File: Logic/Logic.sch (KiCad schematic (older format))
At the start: 8 parts, among them J1 MC_CAN, J12 GPIO_I2C, J2 IMU, J3 RTC, J4 GLV_I2C, J8 GLV_24V

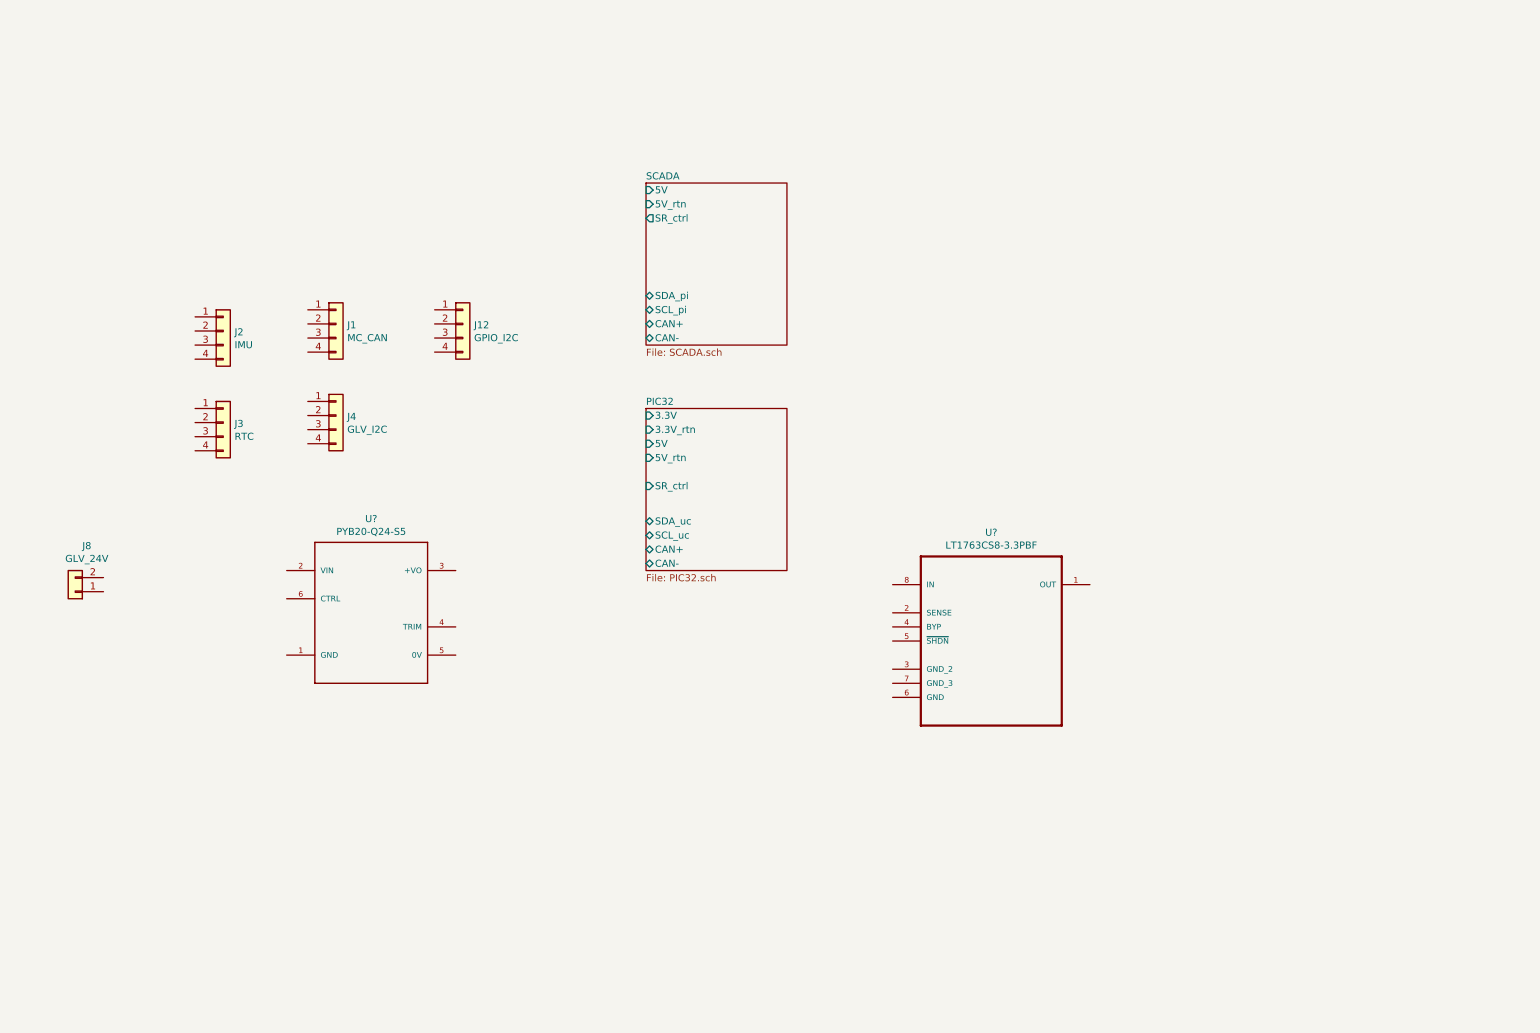
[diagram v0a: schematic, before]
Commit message: Finished Logic Board schematic and removed old schematics
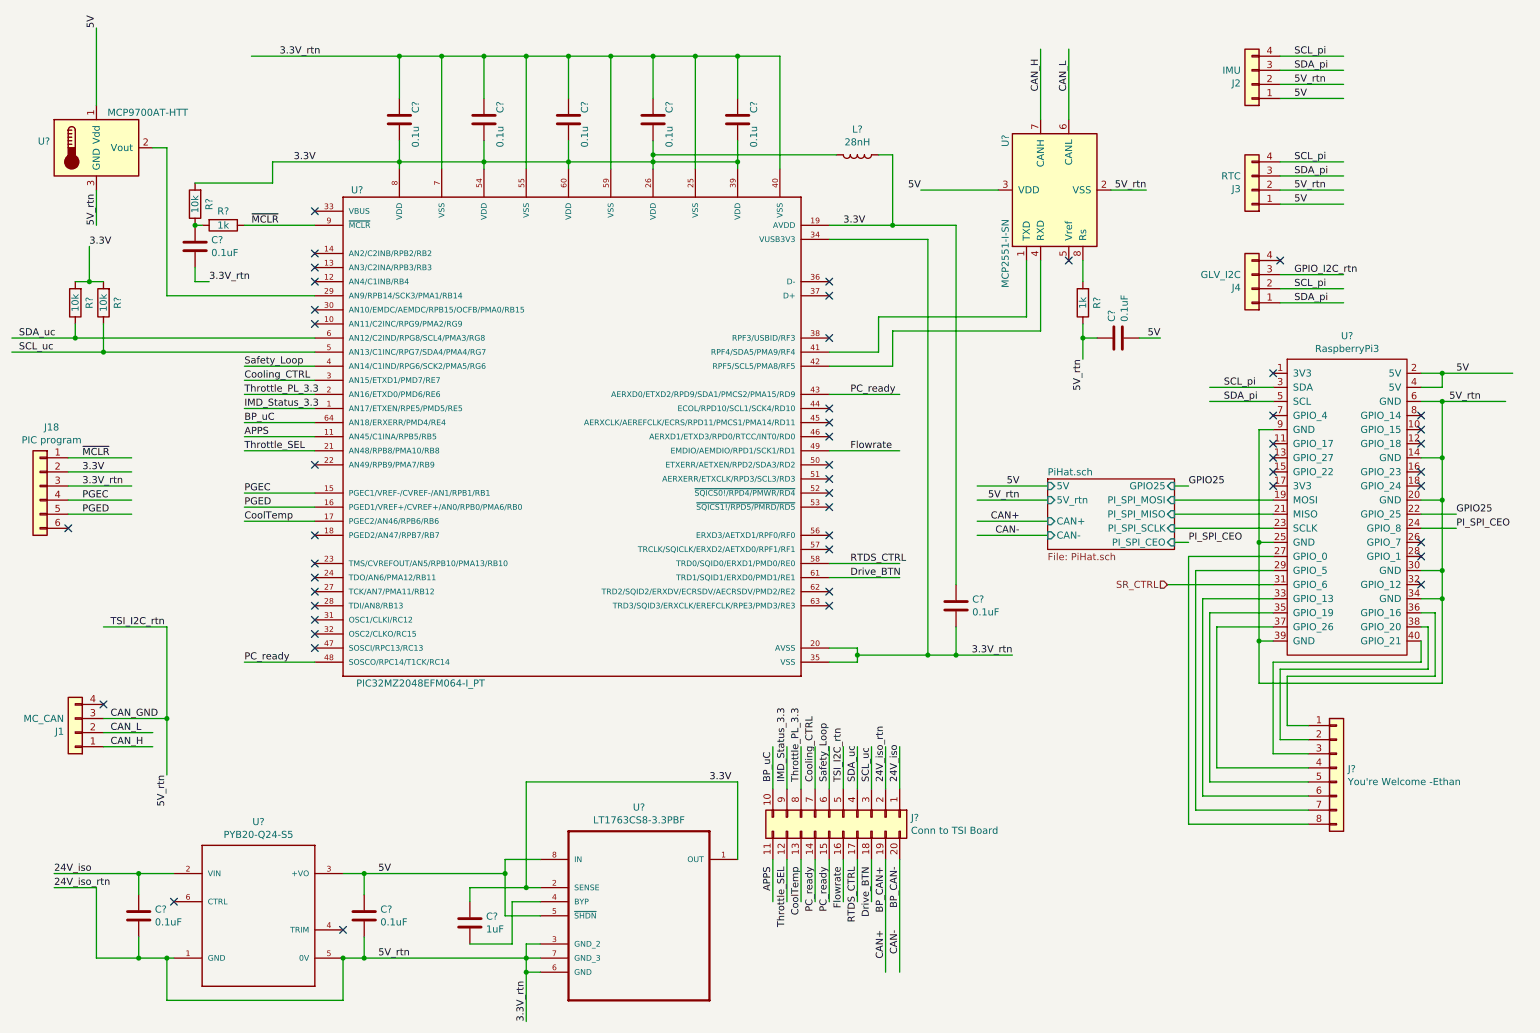
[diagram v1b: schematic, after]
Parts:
- removed J12: GPIO_I2C, symbol Connector_Generic:Conn_01x04
- removed J8: GLV_24V, symbol Connector_Generic:Conn_01x02
- added C? (x5): 0.1uF, symbol Device:C
- added C?: 1uF, symbol Device:C
- added C? (x5): 0.1u, symbol Device:C
- added J18: PIC program, symbol Connector_Generic:Conn_01x06
- added J?: You're Welcome -Ethan, symbol Connector_Generic:Conn_01x08
- added J?: Conn to TSI Board, symbol Connector_Generic:Conn_02x10_Counter_Clockwise
- added L?: 28nH, symbol Device:L
- added R? (x3): 10k, symbol Device:R
- added R? (x2): 1k, symbol Device:R
- added U?: RaspberryPi3, Lafayette_Electric_Car_Footprints:RaspberryPi3, symbol Lafayette_Electric_Car_Internals:RaspberryPi3
- added U?: MCP9700AT-HTT, Package_TO_SOT_SMD:SOT-23, symbol Sensor_Temperature:MCP9700AT-HTT
- added U?: MCP2551-I-SN, Package_SO:SOIC-8_3.9x4.9mm_P1.27mm, symbol Interface_CAN_LIN:MCP2551-I-SN
- added U?: PIC32MZ2048EFM064-I_PT, QFP50P1200X1200X120-64N, symbol PIC32MZ2048EFM064-I_PT:PIC32MZ2048EFM064-I_PT
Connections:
- net labels added: 24V_iso, 24V_iso_rtn, 3.3V, 3.3V_rtn, 5V, 5V_rtn, APPS, BP_CAN+, BP_CAN-, BP_uC, CAN+, CAN-, CAN_GND, CAN_H, CAN_L, CoolTemp, Cooling_CTRL, Drive_BTN, Flowrate, GPIO25, GPIO_I2C_rtn, IMD_Status_3.3, PC_ready, PGEC, PGED, PI_SPI_CEO, RTDS_CTRL, SCL_pi, SCL_uc, SDA_pi, SDA_uc, SR_CTRL, Safety_Loop, TSI_I2C_rtn, Throttle_PL_3.3, Throttle_SEL, ~MCLR~
- wire segments 0 -> 248
- no-connect marks 0 -> 49
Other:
- moved on the sheet: J1, J2, J3, J4, U?
